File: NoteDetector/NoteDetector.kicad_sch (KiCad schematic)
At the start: 24 parts, among them J1 Conn_02x03, J3 Conn_01x01, J4 Conn_01x01, Q1 Q_NMOS_DGS, U1 VM1010, U2 OPAMP, U3 ATtiny1614-SS

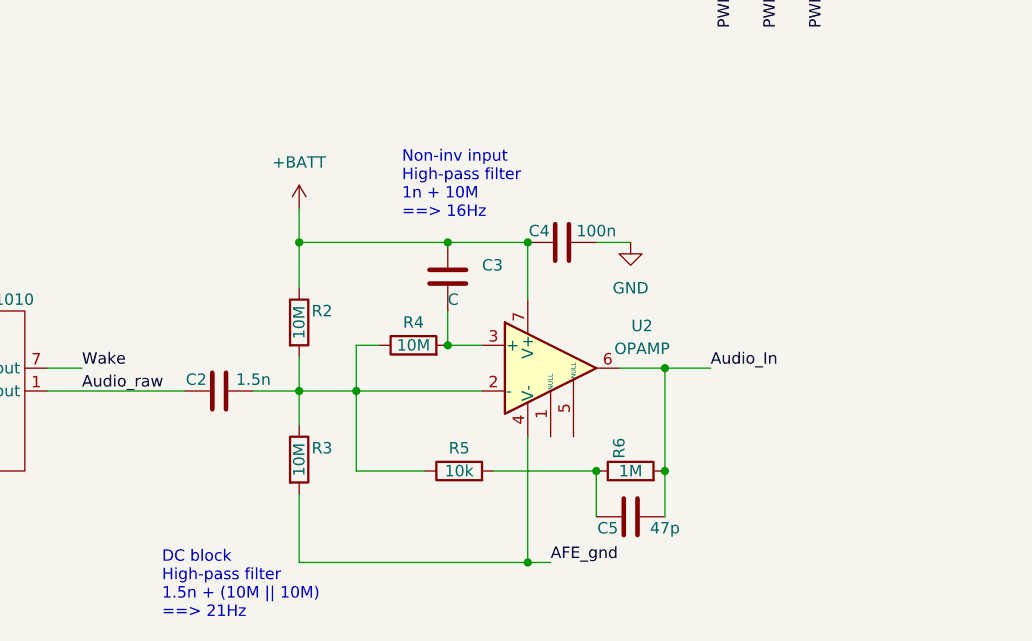
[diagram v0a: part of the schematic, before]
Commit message: Started populating BOM
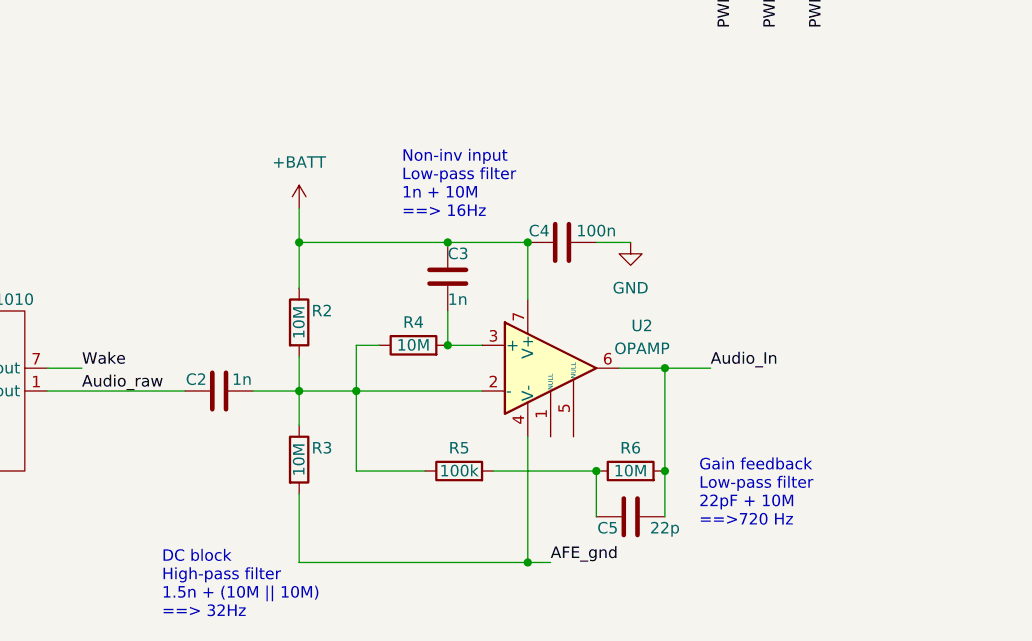
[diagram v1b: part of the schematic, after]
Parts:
- C2: value 1.5n -> 1n
- C3: value C -> 1n
- C5: value 47p -> 22p
- J3, J4: PN (none) -> 5000 (Keystone)
- Q1: PN (none) -> RUC002N05HZGT116
- R2, R3, R4: PN (none) -> RMCF0603FT10M0
- R5: value 10k -> 100k; PN (none) -> RMCF0603FT100K
- R6: value 1M -> 10M; PN (none) -> RMCF0603FT10M0
- U2: PN (none) -> MCP6061-E/SN
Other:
- note added: "DC block High-pass filter 1.5n + (10M || 10M) ==> 32Hz"
- note added: "Gain feedback Low-pass filter 22pF + 10M ==>720 Hz"
- note added: "Non-inv input Low-pass filter 1n + 10M ==> 16Hz"
- note removed: "DC block High-pass filter 1.5n + (10M || 10M) ==> 21Hz"
- note removed: "Non-inv input High-pass filter 1n + 10M ==> 16Hz"
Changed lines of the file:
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@@
     (stroke (width 0) (type default) (color 0 0 0 0))
   )
-  (text "DC block\nHigh-pass filter\n1.5n + (10M || 10M)\n==> 21Hz"
+  (text "Gain feedback\nLow-pass filter\n22pF + 10M\n==>720 Hz"
+    (at 148.59 125.73 0)
+    (effects (font (size 1.27 1.27)) (justify left bottom))
+  )
+  (text "DC block\nHigh-pass filter\n1.5n + (10M || 10M)\n==> 32Hz"
     (at 88.9 135.89 0)
     (effects (font (size 1.27 1.27)) (justify left bottom))
   )
-  (text "Non-inv input\nHigh-pass filter\n1n + 10M\n==> 16Hz" (at 115.57 91.44 0)
+  (text "Non-inv input\nLow-pass filter\n1n + 10M\n==> 16Hz" (at 115.57 91.44 0)
     (effects (font (size 1.27 1.27)) (justify left bottom))
   )
@@
       (effects (font (size 1.27 1.27)) hide)
     )
+    (property "PN" "RMCF0603FT10M0" (id 4) (at 104.14 118.11 0)
+      (effects (font (size 1.27 1.27)) hide)
+    )
     (pin "1")
     (pin "2")
@@
     )
     (property "Datasheet" "http://www.ti.com/lit/ds/symlink/lm741.pdf" (id 3) (at 135.89 104.14 0)
+      (effects (font (size 1.27 1.27)) hide)
+    )
+    (property "PN" "MCP6061-E/SN" (id 4) (at 132.08 107.95 0)
       (effects (font (size 1.27 1.27)) hide)
     )
@@
     )
     (property "Datasheet" "~" (id 3) (at 59.69 40.64 0)
+      (effects (font (size 1.27 1.27)) hide)
+    )
+    (property "PN" "5000 (Keystone)" (id 4) (at 59.69 40.64 0)
       (effects (font (size 1.27 1.27)) hide)
     )
@@
       (effects (font (size 1.27 1.27)) hide)
     )
+    (property "PN" "RMCF0603FT10M0" (id 4) (at 104.14 102.87 0)
+      (effects (font (size 1.27 1.27)) hide)
+    )
     (pin "1")
     (pin "2")
@@
     (in_bom yes) (on_board yes)
     (property "Reference" "R5" (id 0) (at 121.92 116.84 90))
-    (property "Value" "10k" (id 1) (at 121.92 119.38 90))
+    (property "Value" "100k" (id 1) (at 121.92 119.38 90))
     (property "Footprint" "Resistor_SMD:R_0603_1608Metric" (id 2) (at 121.92 121.158 90)
       (effects (font (size 1.27 1.27)) hide)
     )
     (property "Datasheet" "~" (id 3) (at 121.92 119.38 0)
+      (effects (font (size 1.27 1.27)) hide)
+    )
+    (property "PN" "RMCF0603FT100K" (id 4) (at 121.92 119.38 90)
       (effects (font (size 1.27 1.27)) hide)
     )
@@
       (effects (font (size 1.27 1.27)) hide)
     )
+    (property "PN" "RMCF0603FT10M0" (id 4) (at 116.84 105.41 0)
+      (effects (font (size 1.27 1.27)) hide)
+    )
     (pin "1")
     (pin "2")
@@
   (symbol (lib_id "Device:R") (at 140.97 119.38 90) (unit 1)
     (in_bom yes) (on_board yes)
-    (property "Reference" "R6" (id 0) (at 139.6999 116.84 0))
-    (property "Value" "1M" (id 1) (at 140.97 119.38 90))
+    (property "Reference" "R6" (id 0) (at 140.97 116.84 90))
+    (property "Value" "10M" (id 1) (at 140.97 119.38 90))
     (property "Footprint" "Resistor_SMD:R_0603_1608Metric" (id 2) (at 140.97 121.158 90)
       (effects (font (size 1.27 1.27)) hide)
     )
     (property "Datasheet" "~" (id 3) (at 140.97 119.38 0)
+      (effects (font (size 1.27 1.27)) hide)
+    )
+    (property "PN" "RMCF0603FT10M0" (id 4) (at 140.97 119.38 0)
       (effects (font (size 1.27 1.27)) hide)
     )
@@
     (in_bom yes) (on_board yes)
     (property "Reference" "C2" (id 0) (at 92.71 109.22 90))
-    (property "Value" "1.5n" (id 1) (at 99.06 109.22 90))
+    (property "Value" "1n" (id 1) (at 97.79 109.22 90))
     (property "Footprint" "Capacitor_SMD:C_0603_1608Metric" (id 2) (at 99.06 109.5248 0)
       (effects (font (size 1.27 1.27)) hide)
@@
       (effects (font (size 1.27 1.27)) hide)
     )
+    (property "PN" "RUC002N05HZGT116" (id 4) (at 208.28 110.49 0)
+      (effects (font (size 1.27 1.27)) hide)
+    )
     (pin "1")
     (pin "2")
@@
   (symbol (lib_id "Device:C") (at 120.65 97.79 180) (unit 1)
     (in_bom yes) (on_board yes)
-    (property "Reference" "C3" (id 0) (at 124.46 96.5199 0)
+    (property "Reference" "C3" (id 0) (at 120.65 95.25 0)
       (effects (font (size 1.27 1.27)) (justify right))
     )
-    (property "Value" "C" (id 1) (at 120.65 100.33 0)
+    (property "Value" "1n" (id 1) (at 120.65 100.33 0)
       (effects (font (size 1.27 1.27)) (justify right))
     )
@@
       (effects (font (size 1.27 1.27)) hide)
     )
+    (property "PN" "5000 (Keystone)" (id 4) (at 59.69 34.29 0)
+      (effects (font (size 1.27 1.27)) hide)
+    )
     (pin "1")
   )
@@
     (in_bom yes) (on_board yes)
     (property "Reference" "C5" (id 0) (at 138.43 125.73 90))
-    (property "Value" "47p" (id 1) (at 144.78 125.73 90))
+    (property "Value" "22p" (id 1) (at 144.78 125.73 90))
     (property "Footprint" "Capacitor_SMD:C_0603_1608Metric" (id 2) (at 137.16 125.4252 0)
       (effects (font (size 1.27 1.27)) hide)
@@
     )
     (path "/af05a1af-cacc-4b31-86ff-7a3359c0aafb"
-      (reference "C2") (unit 1) (value "1.5n") (footprint "Capacitor_SMD:C_0603_1608Metric")
+      (reference "C2") (unit 1) (value "1n") (footprint "Capacitor_SMD:C_0603_1608Metric")
     )
     (path "/dfa41b1f-5700-4ccb-a86f-22d86067b4ff"
-      (reference "C3") (unit 1) (value "C") (footprint "Capacitor_SMD:C_0603_1608Metric")
+      (reference "C3") (unit 1) (value "1n") (footprint "Capacitor_SMD:C_0603_1608Metric")
     )
     (path "/e553ddf9-aab9-4f15-817b-d418042fa2b4"
@@
     )
     (path "/f4589a73-a36d-4d6f-86cf-7c4cb1ba003a"
-      (reference "C5") (unit 1) (value "47p") (footprint "Capacitor_SMD:C_0603_1608Metric")
+      (reference "C5") (unit 1) (value "22p") (footprint "Capacitor_SMD:C_0603_1608Metric")
     )
     (path "/eb828bfa-f37b-4838-a8dd-4fc0d4a13f32"
@@
     )
     (path "/55a0bc72-c349-40a8-8b3b-92a8a5261817"
-      (reference "R5") (unit 1) (value "10k") (footprint "Resistor_SMD:R_0603_1608Metric")
+      (reference "R5") (unit 1) (value "100k") (footprint "Resistor_SMD:R_0603_1608Metric")
     )
     (path "/78c44ba8-ab44-48aa-9ac6-060a333181f6"
-      (reference "R6") (unit 1) (value "1M") (footprint "Resistor_SMD:R_0603_1608Metric")
+      (reference "R6") (unit 1) (value "10M") (footprint "Resistor_SMD:R_0603_1608Metric")
     )
     (path "/b6426b7d-54b8-4a66-86d3-f239ed13caa4"

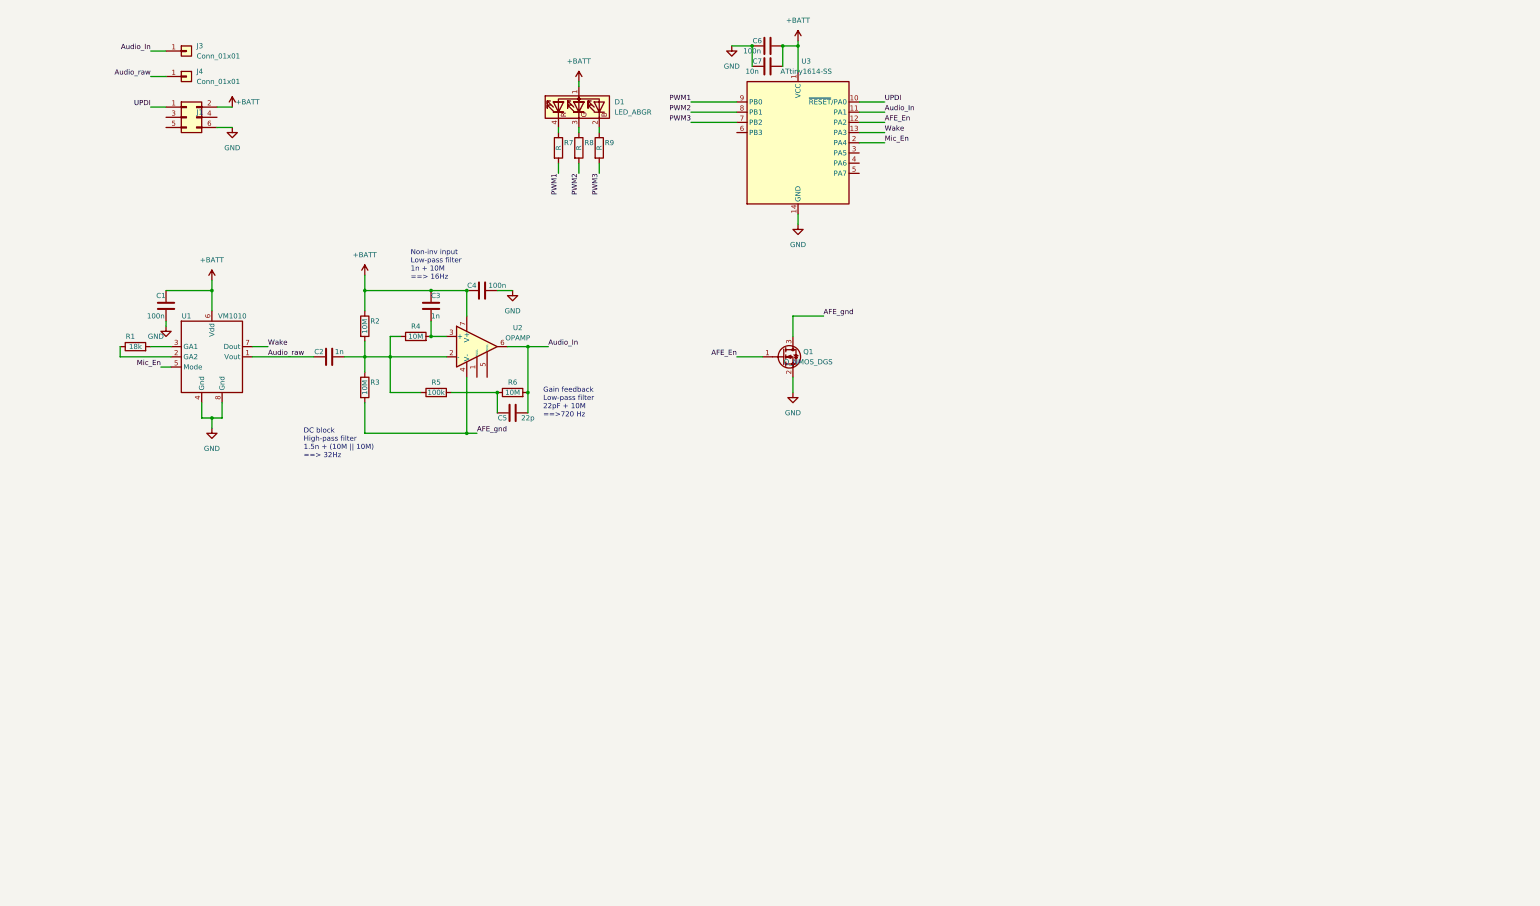
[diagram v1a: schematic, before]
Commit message: changed amp circuit
replacing MEMS mic with electret condenser
Todo: new microcontroller
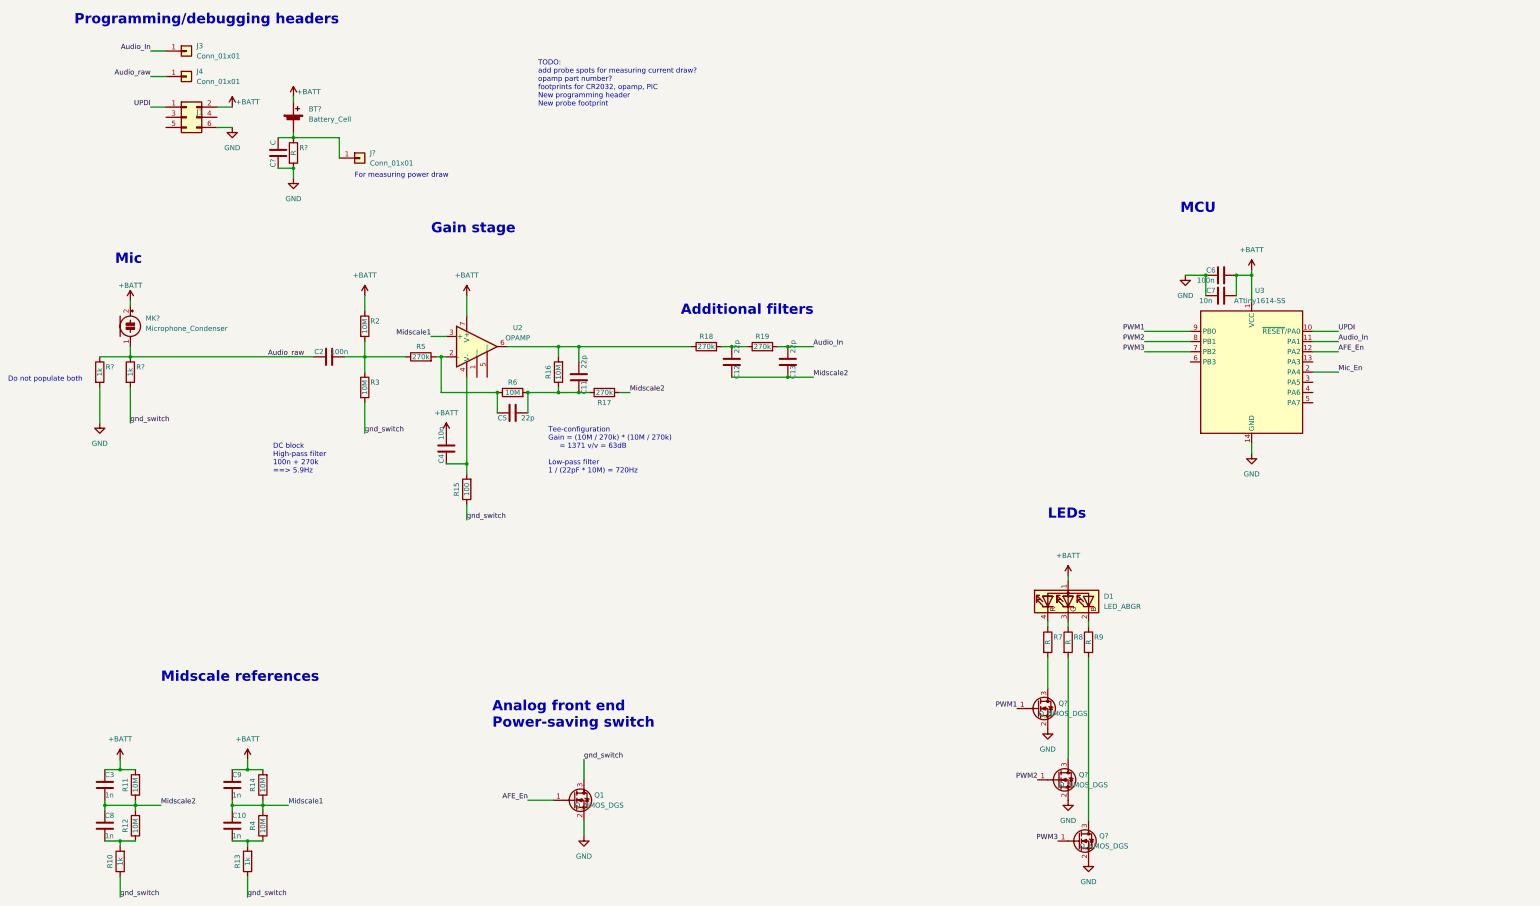
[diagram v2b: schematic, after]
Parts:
- removed C1: 100n, Capacitor_SMD:C_0603_1608Metric, symbol Device:C
- removed R1: 18k, Resistor_SMD:R_0603_1608Metric, symbol Device:R
- removed U1: VM1010, User:MEMS_mic_VS1010, symbol user:VM1010
- added BT?: Battery_Cell, symbol Device:Battery_Cell
- added C10, C8, C9: 1n, Capacitor_SMD:C_0603_1608Metric, symbol Device:C
- added C11, C12, C13: 22p, Capacitor_SMD:C_0603_1608Metric, symbol Device:C
- added C?: C, Capacitor_SMD:C_0603_1608Metric, symbol Device:C
- added J?: Conn_01x01, TestPoint:TestPoint_Loop_D2.50mm_Drill1.0mm, symbol Connector_Generic:Conn_01x01
- added MK?: Microphone_Condenser, symbol Device:Microphone_Condenser
- added Q? (x3): Q_NMOS_DGS, Package_TO_SOT_SMD:SOT-23, symbol Device:Q_NMOS_GSD
- added R10, R13, R? (x2): 1k, Resistor_SMD:R_0603_1608Metric, symbol Device:R
- added R11, R12, R14, R16: 10M, Resistor_SMD:R_0603_1608Metric, symbol Device:R
- added R15: 100, Resistor_SMD:R_0603_1608Metric, symbol Device:R
- added R17, R18, R19: 270k, Resistor_SMD:R_0603_1608Metric, symbol Device:R
- added R?: R, Resistor_SMD:R_0603_1608Metric, symbol Device:R
- C2: value 1n -> 100n
- C4: value 100n -> 10n
- R5: value 100k -> 270k; PN RMCF0603FT100K -> (none)
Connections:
- net +BATT: now also C4.1, BT?.1 (+), C9.2, MK?.2 (+), R11.2, R14.2; no longer C4.2
- net Audio_In: now also C13.1, R19.2; no longer C5.1, R6.2, U2.6
- net Audio_raw: now also MK?.1 (-), R?.1, R?.1
- net GND: now also C?.1, Q?.2 (S), Q?.2 (S), Q?.2 (S), R?.2, R?.2; no longer C4.1
- net PWM1: now also Q?.1 (G); no longer R7.2
- net PWM2: now also Q?.1 (G); no longer R8.2
- net PWM3: now also Q?.1 (G); no longer R9.2
- net at C2.2, R2.2, R3.1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: no longer R4.1, U2.2 (-)
- net Midscale1: now reaches R4.2, U2.3 (+)
- net Midscale1: now also C10.2, C9.1, R14.1; no longer C3.1
- net at C5.2, R5.2, R6.1: now also U2.2 (-)
- net AFE_gnd renamed gnd_switch
- net gnd_switch: now also R10.1, R13.1, R15.1, R?.2; no longer U2.4 (V-)
- net Wake: no longer names the net of U3.13 (PA3)
- new net: BT?.2 (-), C?.2, J?.1 (Pin_1), R?.1
- new net: Q?.3 (D), R8.2
- new net: C11.2, C5.1, R16.1, R17.1, R6.2
- new net: C11.1, R16.2, R18.1, U2.6
- new net: C8.1, R10.2, R12.1
- new net: C4.2, R15.2, U2.4 (V-)
- new net: Q?.3 (D), R9.2
- new net: C10.1, R13.2, R4.1
- new net: C12.1, R18.2, R19.1
- new net: Q?.3 (D), R7.2
- new net Midscale2: C12.2, C13.2, C3.1, C8.2, R11.1, R12.2, R17.2
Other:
- note added: "Additional filters"
- note added: "Analog front end Power-saving switch"
- note added: "DC block High-pass filter 100n + 270k ==> 5.9Hz"
- note added: "Do not populate both"
- note added: "For measuring power draw"
- note added: "Gain stage"
- note added: "LEDs"
- note added: "MCU"
- note added: "Mic"
- note added: "Midscale references"
- note added: "Programming/debugging headers"
- note added: "TODO: add probe spots for measuring current draw? opamp part number? footprints for CR2032, opamp, PIC New programming header New probe footprint"
- note added: "Tee-configuration Gain = (10M / 270k) * (10M / 270k) = 1371 v/v = 63dB Low-pass filter 1 / (22pF * 10M) = 720Hz"
- note removed: "DC block High-pass filter 1.5n + (10M || 10M) ==> 32Hz"
- note removed: "Gain feedback Low-pass filter 22pF + 10M ==>720 Hz"
- note removed: "Non-inv input Low-pass filter 1n + 10M ==> 16Hz"
- moved on the sheet: C4, C6, C7, D1, Q1, R4, R5, R7, R8, R9, U3
